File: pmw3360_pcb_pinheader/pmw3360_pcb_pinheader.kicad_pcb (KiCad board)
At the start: 2 copper layers, 23.5 x 33 mm, 20 parts, among them J1 Conn_01x08, U1 PMW3360DM-T2QU, U2 TPS73601DBV

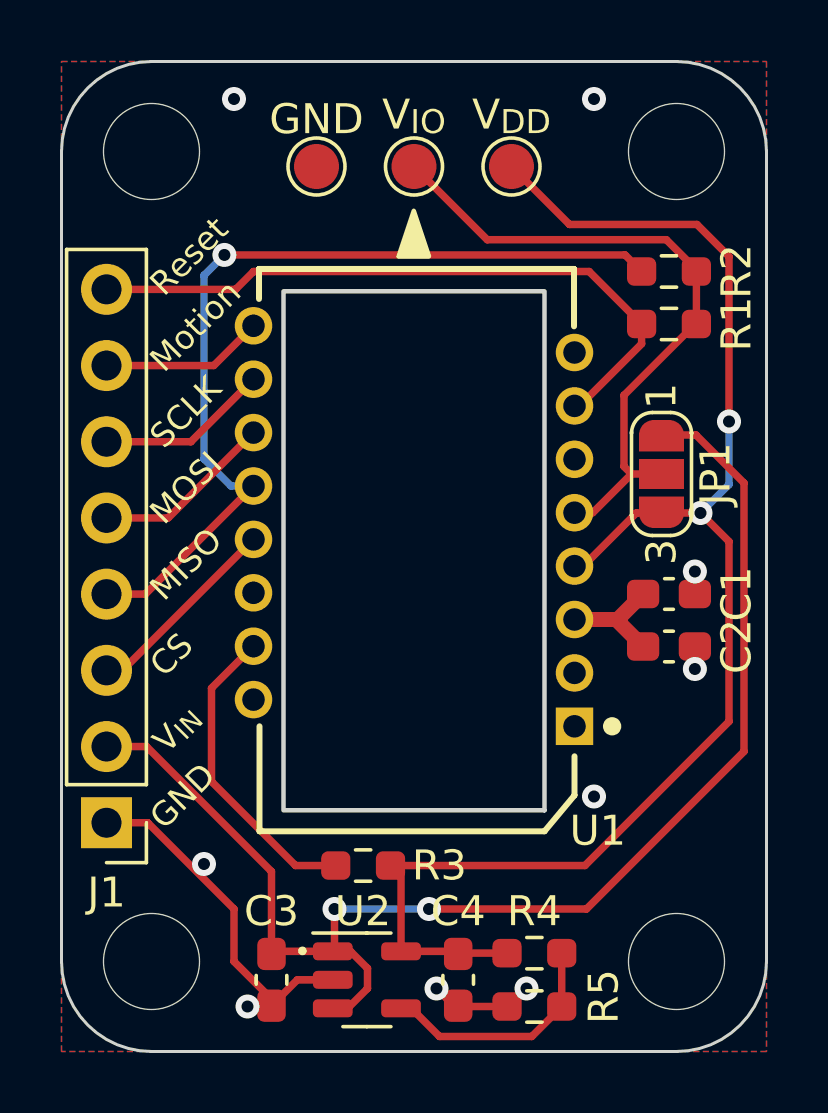
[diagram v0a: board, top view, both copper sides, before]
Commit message: Change pin header edition LDO to TLV74318PDBVR
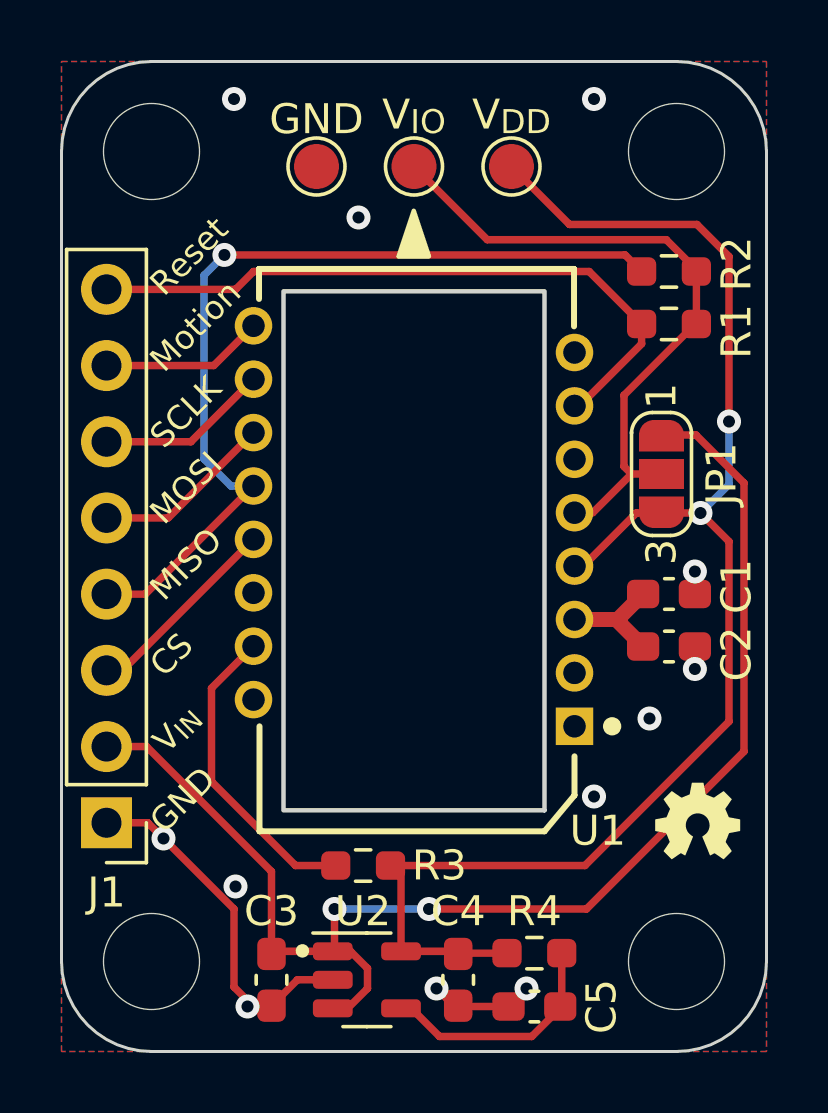
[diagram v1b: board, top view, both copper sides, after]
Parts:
- removed R5: 56.2k, Resistor_SMD:R_0603_1608Metric_Pad0.98x0.95mm_HandSolder
- added C5: 22nF, Capacitor_SMD:C_0603_1608Metric_Pad1.08x0.95mm_HandSolder, F.Cu at (149.7, 108.0)
- C4: value 4.7uF -> 1uF
- TP1: value VIO TestPoint -> VIO
- TP2: value VDD TestPoint -> VDD
- TP3: value GND TestPoint -> GND
- U2: value TPS73601DBV -> TLV74318PDBVR
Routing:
- net GND: track 15.1 -> 15.4 mm, vias 9 -> 12
